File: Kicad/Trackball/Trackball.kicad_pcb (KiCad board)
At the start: 2 copper layers, 83.3 x 111.2 mm, 15 parts, among them J1 52559-1233, J2 Conn_01x04_Male, J3 Conn_01x04_Male, J4 Conn_01x04_Male, J5 Conn_01x04_Male, J6 Conn_01x04_Male, J7 Conn_01x04_Male, J8 Conn_01x04_Male, J9 Conn_01x04_Male, U1 ProMicro

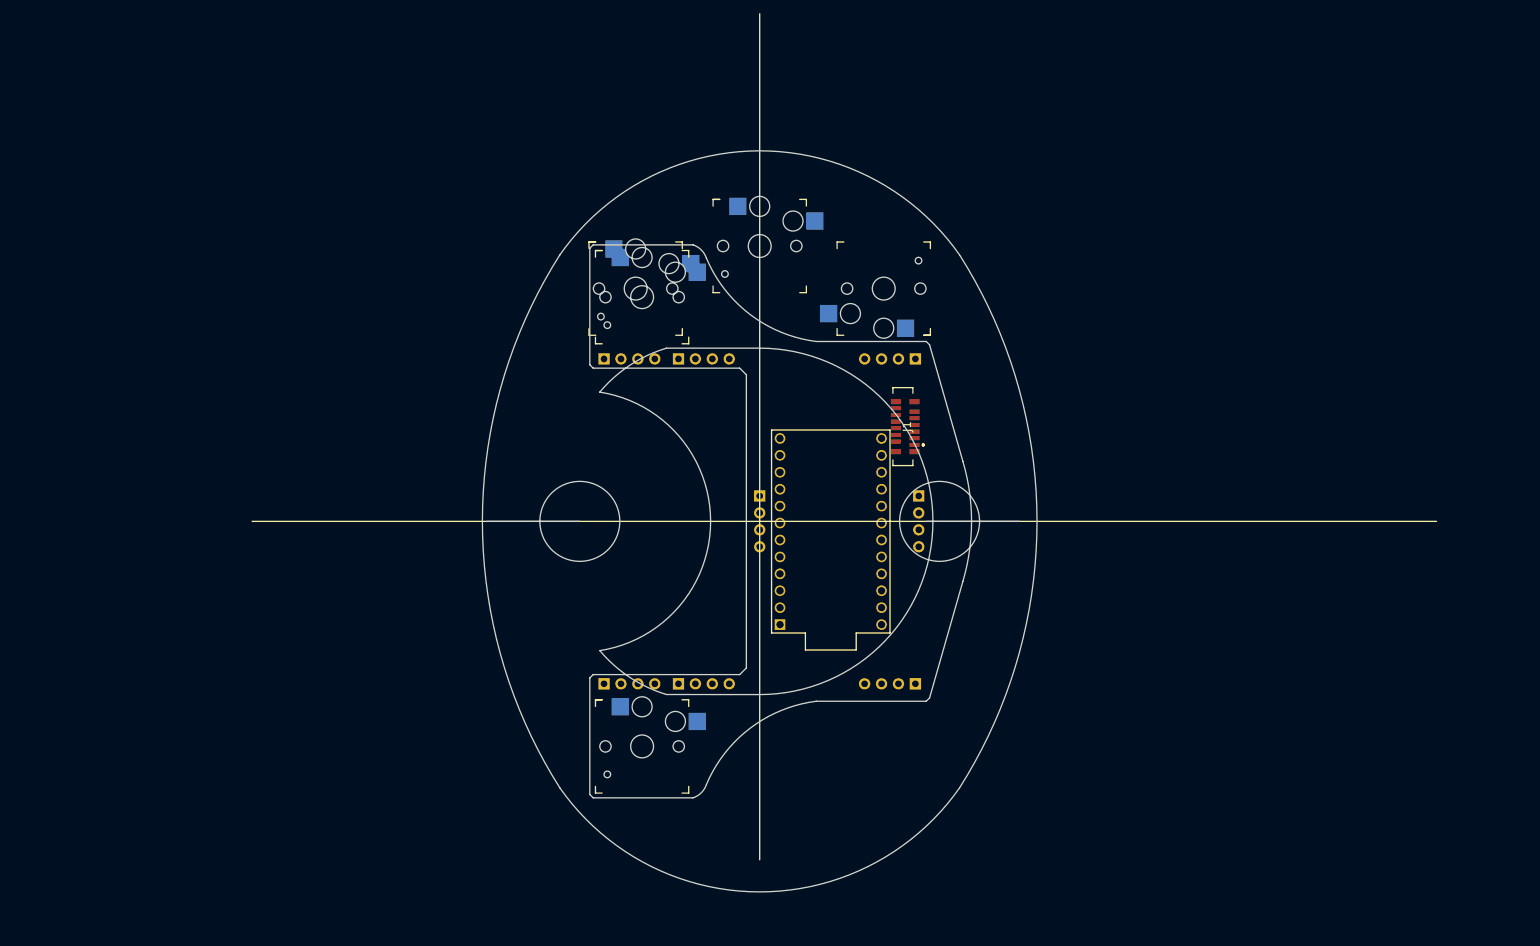
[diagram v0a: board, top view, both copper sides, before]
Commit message: Started laying out the schematics and traces.
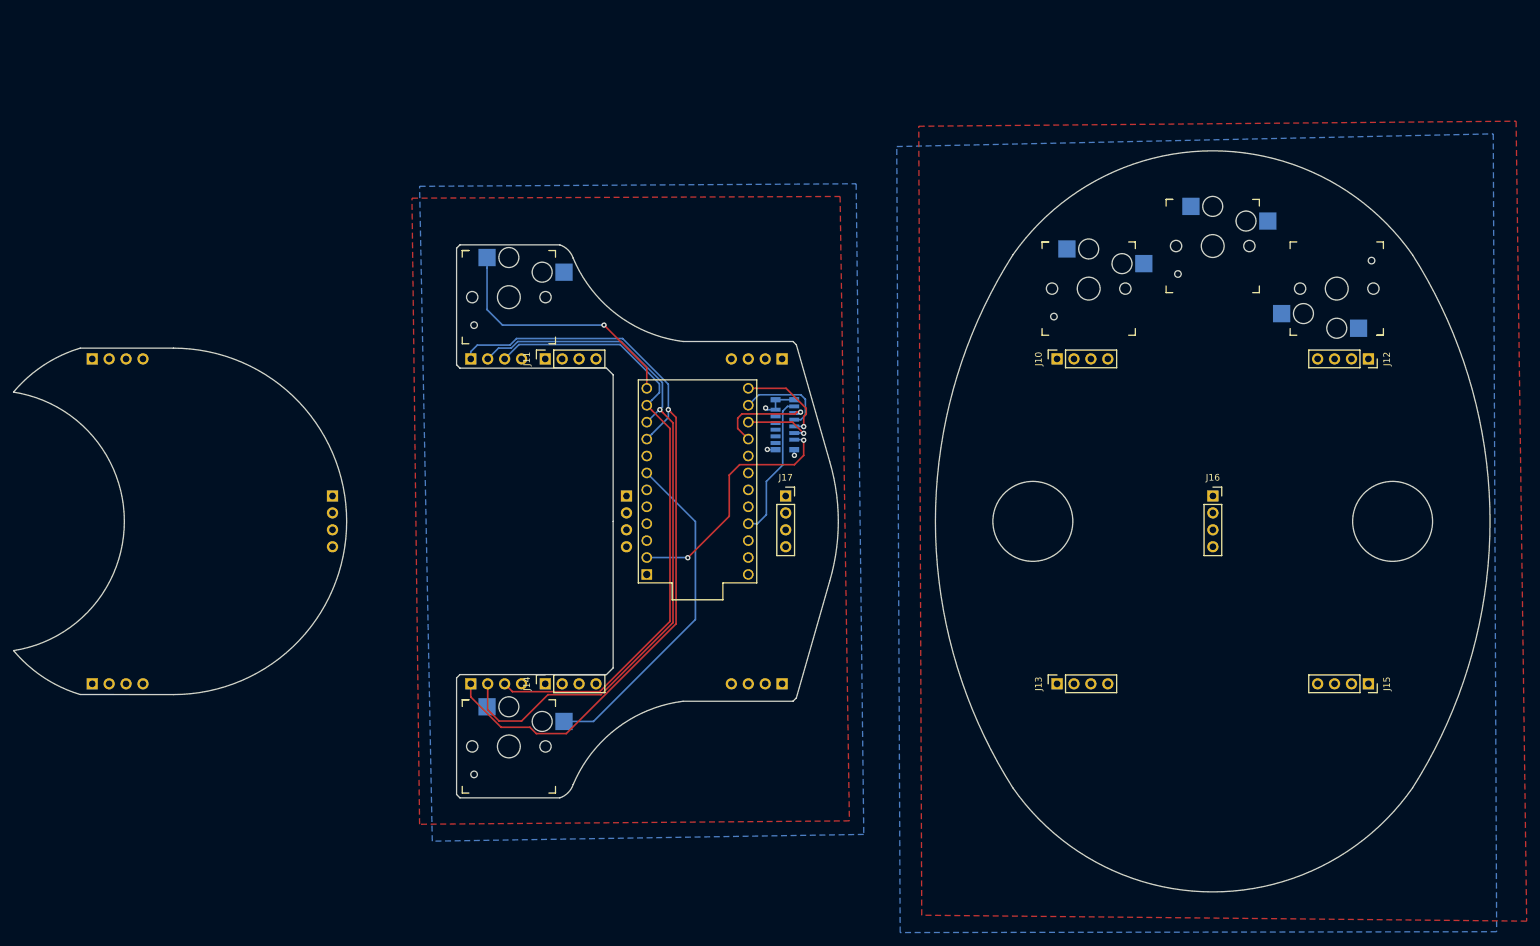
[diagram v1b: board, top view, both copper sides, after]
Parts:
- added J10: Conn_01x04_Female, Connector_PinSocket_2.54mm:PinSocket_1x04_P2.54mm_Vertical, F.Cu at (197.0, 77.2)
- added J11: Conn_01x04_Female, Connector_PinSocket_2.54mm:PinSocket_1x04_P2.54mm_Vertical, F.Cu at (120.2, 77.2)
- added J12: Conn_01x04_Female, Connector_PinSocket_2.54mm:PinSocket_1x04_P2.54mm_Vertical, F.Cu at (243.8, 77.2)
- added J13: Conn_01x04_Female, Connector_PinSocket_2.54mm:PinSocket_1x04_P2.54mm_Vertical, F.Cu at (197.0, 126.0)
- added J14: Conn_01x04_Female, Connector_PinSocket_2.54mm:PinSocket_1x04_P2.54mm_Vertical, F.Cu at (120.2, 126.0)
- added J15: Conn_01x04_Female, Connector_PinSocket_2.54mm:PinSocket_1x04_P2.54mm_Vertical, F.Cu at (243.8, 126.0)
- added J16: Conn_01x04_Female, Connector_PinSocket_2.54mm:PinSocket_1x04_P2.54mm_Vertical, F.Cu at (220.4, 97.8)
- added J17: Conn_01x04_Female, Connector_PinSocket_2.54mm:PinSocket_1x04_P2.54mm_Vertical, F.Cu at (156.3, 97.8)
- J1: moved to B.Cu
- moved J9 88.0 mm to (88.3, 97.8)
- moved J7 88.0 mm to (52.2, 77.2)
- moved J8 88.0 mm to (52.2, 126.0)
- moved MX1 68.0 mm to (201.8, 66.7)
- moved MX2 68.0 mm to (220.4, 60.3)
- moved MX3 68.0 mm to (239.0, 66.7)
- moved U1 21.4 mm to (143.1, 95.6)
- moved J2 20.0 mm to (109.0, 77.2)
- moved J3 20.0 mm to (109.0, 126.0)
- moved MX4 20.0 mm to (114.7, 135.4)
- moved MX5 20.0 mm to (114.7, 67.9)
- moved J4 20.0 mm to (155.8, 77.2)
- moved J5 20.0 mm to (155.8, 126.0)
- moved J6 20.0 mm to (132.4, 97.8)
- moved J1 18.1 mm to (156.2, 87.1)
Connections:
- J1 pad 1: GND -> (no net)
- J1 pad 10: (no net) -> NCS
- J1 pad 11: (no net) -> GND
- J1 pad 12: (no net) -> +3V3
- J1 pad 2: (no net) -> MOTION
- J1 pad 4: (no net) -> SCLK
- J1 pad 6: (no net) -> MOSI
- J1 pad 8: (no net) -> MISO
- J2 pad 1: (no net) -> Button1
- J2 pad 2: (no net) -> Button2
- J2 pad 3: (no net) -> Button3
- J2 pad 4: (no net) -> GND
- J3 pad 1: (no net) -> Button1
- J3 pad 2: (no net) -> Button2
- J3 pad 3: (no net) -> Button3
- J3 pad 4: (no net) -> GND
- MX1 pad 1: (no net) -> Net-(J10-Pad1)
- MX1 pad 2: (no net) -> Net-(MX1-Pad2)
- MX2 pad 1: (no net) -> Net-(J10-Pad2)
- MX2 pad 2: (no net) -> Net-(MX1-Pad2)
- MX3 pad 1: (no net) -> Net-(J10-Pad3)
- MX3 pad 2: (no net) -> Net-(MX1-Pad2)
- MX4 pad 1: (no net) -> GND
- MX4 pad 2: (no net) -> Button4
- MX5 pad 1: (no net) -> Button5
- MX5 pad 2: (no net) -> GND
- U1 pad 10: (no net) -> Button2
- U1 pad 11: (no net) -> Button3
- U1 pad 12: (no net) -> Button5
- U1 pad 13: (no net) -> MOSI
- U1 pad 14: (no net) -> MISO
- U1 pad 15: (no net) -> SCLK
- U1 pad 16: (no net) -> NCS
- U1 pad 2: (no net) -> MOTION
- U1 pad 21: (no net) -> +3V3
- U1 pad 23: (no net) -> GND
- U1 pad 3: (no net) -> GND
- U1 pad 4: (no net) -> GND
- U1 pad 7: (no net) -> Button4
- U1 pad 9: (no net) -> Button1
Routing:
- net Button1: track 0.00 -> 118.5 mm, vias 0 -> 1
- net Button2: track 0.00 -> 108.1 mm, vias 0 -> 1
- net Button3: track 0.00 -> 94.1 mm
- net Button4: track 0.00 -> 51.1 mm
- net Button5: track 0.00 -> 38.5 mm, vias 0 -> 1
- net MOTION: track 0.00 -> 37.4 mm, vias 0 -> 2
- net +3V3: track 0.00 -> 21.8 mm
- net NCS: track 0.00 -> 14.6 mm, vias 0 -> 1
- net MOSI: track 0.00 -> 14.3 mm, vias 0 -> 1
- net MISO: track 0.00 -> 13.8 mm
- net SCLK: track 0.00 -> 10.5 mm, vias 0 -> 1
- net GND: track 0.00 -> 8.01 mm, vias 0 -> 3
- added copper zone on B.Cu, net GND
- added copper zone on F.Cu, net GND
- added copper zone on B.Cu, net GNDA
- added copper zone on F.Cu, net GNDA
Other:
- board size 83.3 x 111.2 mm -> 221.6 x 111.2 mm
